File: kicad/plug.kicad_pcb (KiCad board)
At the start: 2 copper layers, 11 parts, among them J1 74320-1004, P1 HDMI_RECEPTACLE

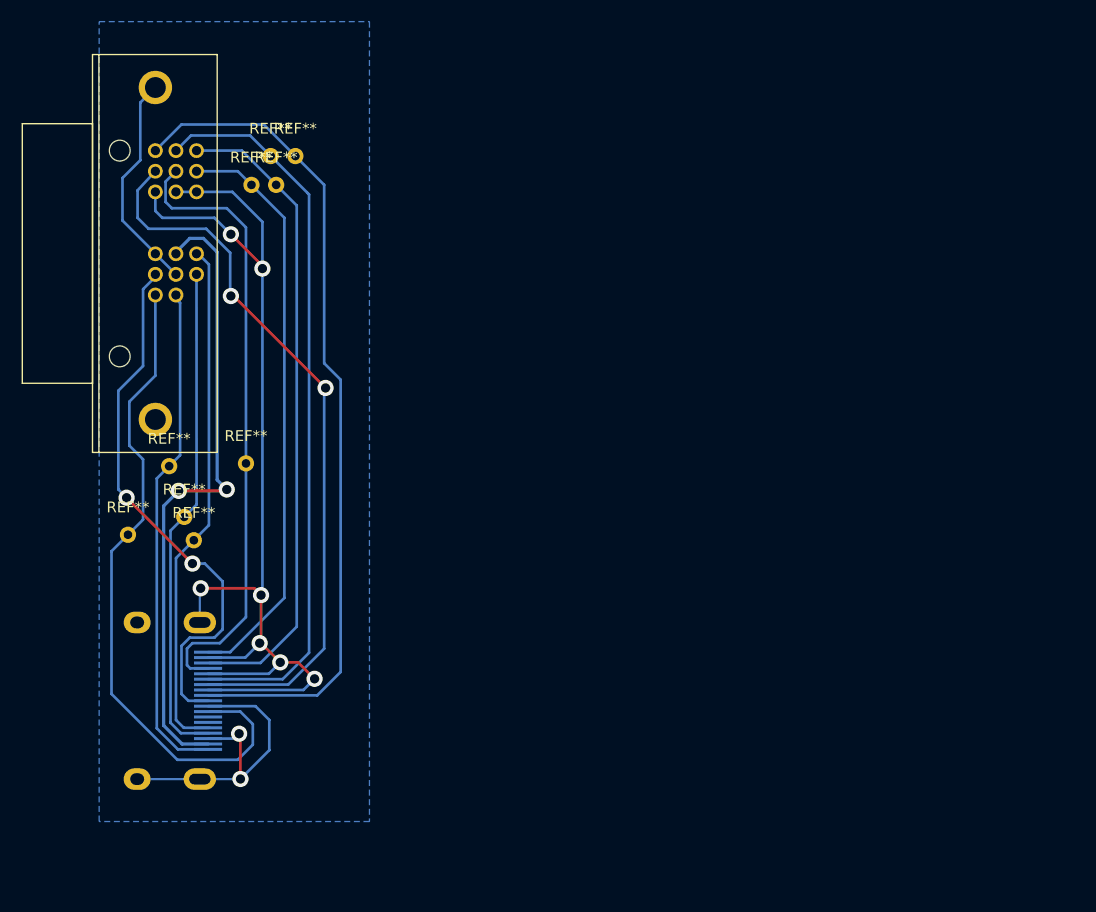
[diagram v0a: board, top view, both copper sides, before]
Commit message: simplier version since hdmi is a pain to manage.
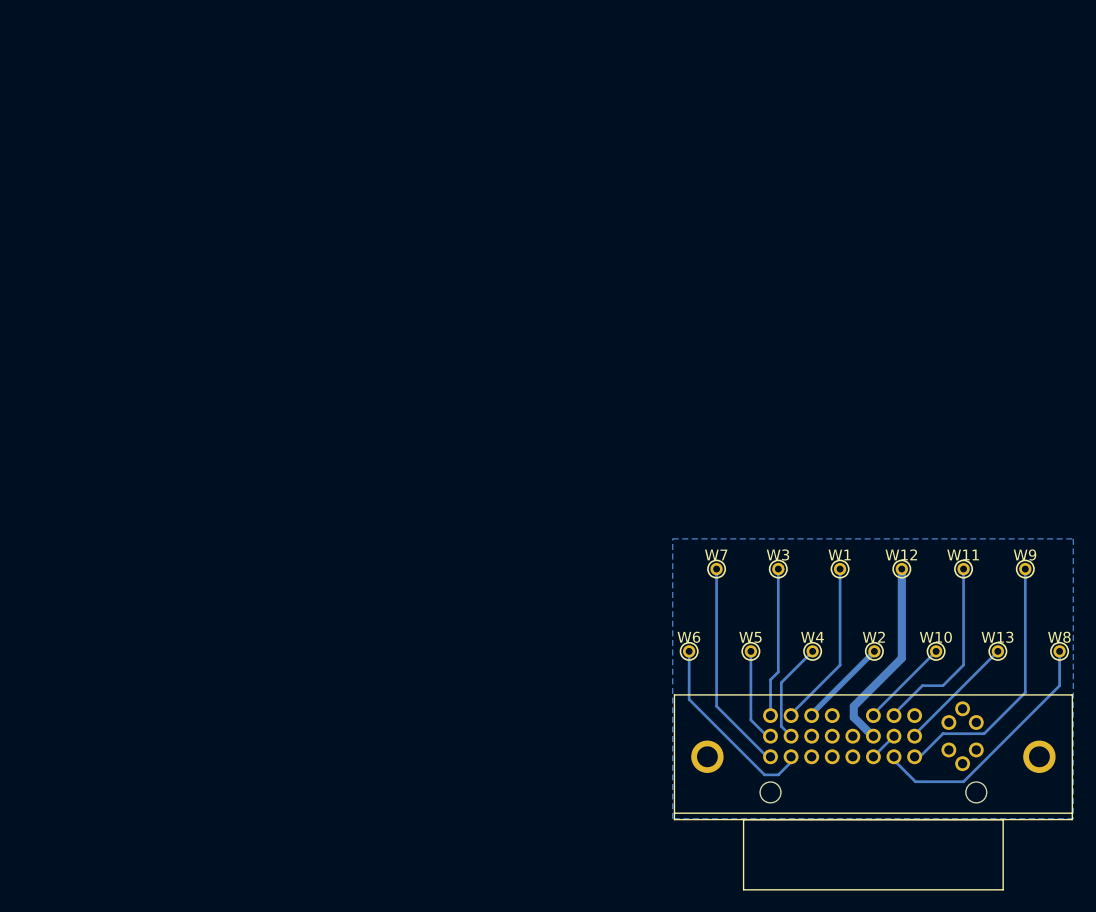
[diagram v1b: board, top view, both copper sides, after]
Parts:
- removed P1: HDMI_RECEPTACLE, project:HDMI_SMD
- removed REF** (x9): Measurement_Point_Round-TH_Small, Measurement_Points:Measurement_Point_Round-TH_Small
- added W1: TEST_1P, Connectors:PINTST, F.Cu at (154.9, 91.4)
- added W10: TEST_1P, Connectors:PINTST, F.Cu at (163.8, 99.1)
- added W11: TEST_1P, Connectors:PINTST, F.Cu at (166.4, 91.4)
- added W12: TEST_1P, Connectors:PINTST, F.Cu at (160.7, 91.4)
- added W13: TEST_1P, Connectors:PINTST, F.Cu at (169.5, 99.1)
- added W2: TEST_1P, Connectors:PINTST, F.Cu at (158.1, 99.1)
- added W3: TEST_1P, Connectors:PINTST, F.Cu at (149.2, 91.4)
- added W4: TEST_1P, Connectors:PINTST, F.Cu at (152.4, 99.1)
- added W5: TEST_1P, Connectors:PINTST, F.Cu at (146.7, 99.1)
- added W6: TEST_1P, Connectors:PINTST, F.Cu at (141.0, 99.1)
- added W7: TEST_1P, Connectors:PINTST, F.Cu at (143.5, 91.4)
- added W8: TEST_1P, Connectors:PINTST, F.Cu at (175.3, 99.1)
- added W9: TEST_1P, Connectors:PINTST, F.Cu at (172.1, 91.4)
- moved J1 73.9 mm to (148.5, 105.0), turned to 0 degrees
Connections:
- J1 pad 11: /GND -> GND
- J1 pad 15: /GND -> GND
- J1 pad 19: /GND -> GND
- J1 pad 22: /GND -> GND
- J1 pad 25: /GND -> GND
- J1 pad 3: /GND -> GND
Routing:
- net /GND: track 151.0 -> 0.00 mm, vias 9 -> 0
- net /D1-: track 67.9 -> 8.79 mm
- net /D0-: track 77.8 -> 19.6 mm
- net /D0+: track 67.7 -> 17.8 mm, vias 2 -> 0
- net /D1+: track 58.1 -> 9.43 mm
- net /D2-: track 59.8 -> 13.9 mm
- net /+5v: track 59.0 -> 18.1 mm, vias 2 -> 0
- net /DDCcl: track 48.4 -> 8.35 mm
- net /D2+: track 54.2 -> 15.4 mm
- net /CL-: track 62.2 -> 24.1 mm
- net /hotplug: track 46.8 -> 11.0 mm
- net /DDCdata: track 46.5 -> 17.3 mm
- net /CL+: track 51.9 -> 23.3 mm, vias 2 -> 0
- net GND: track 0.00 -> 11.0 mm
- added copper zone on B.Cu, net GND
- removed copper zone on B.Cu, net /GND
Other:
- net class 5v: trace_width 0.3 -> 0.75
- net class GND added: clearance 0, trace_width 0.5, via_dia 1.50114, via_drill 0.86106

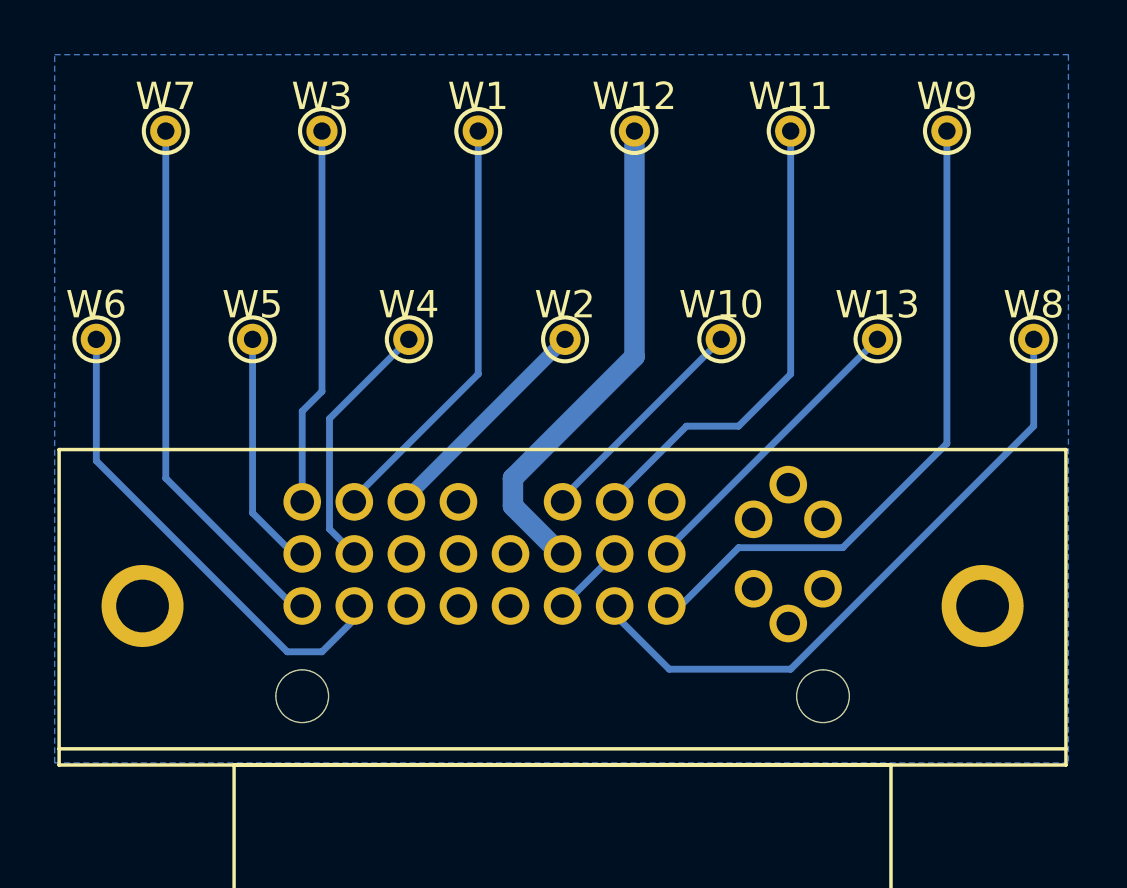
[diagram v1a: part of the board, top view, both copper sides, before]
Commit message: added pad footprint
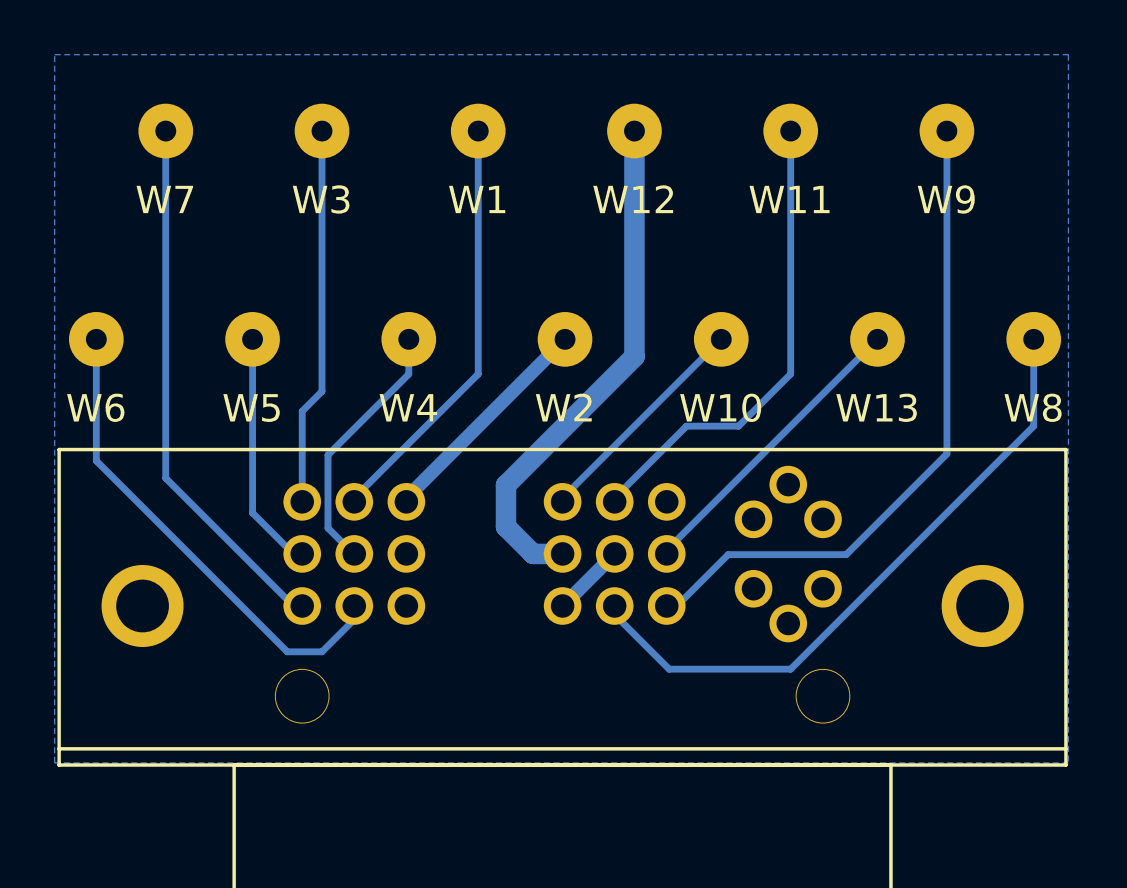
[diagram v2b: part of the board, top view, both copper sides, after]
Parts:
- W1, W10, W11, W12, W13, W2, W3, W4, W5, W6, W7, W8, W9: footprint Connectors:PINTST -> project:pad
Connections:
- J1 pad : (no net) -> GND
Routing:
- net /+5v: track 18.1 -> 19.0 mm

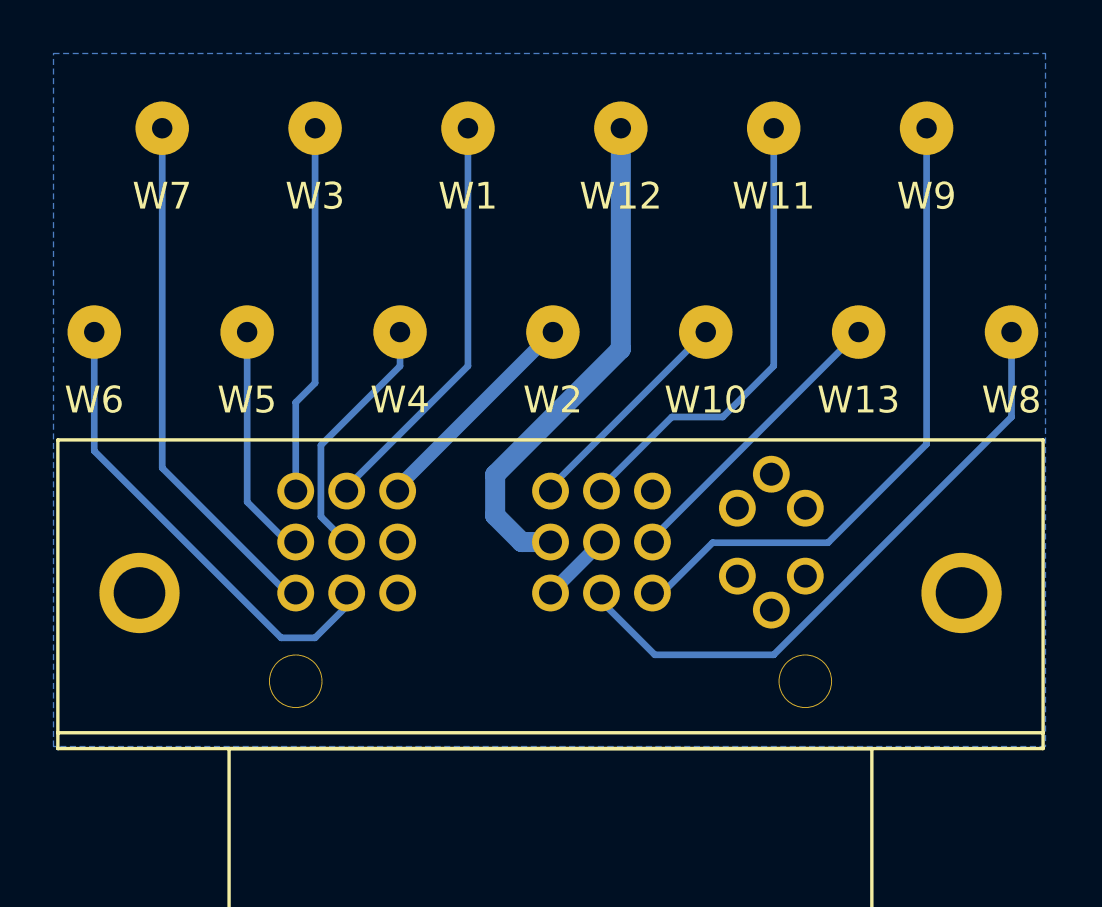
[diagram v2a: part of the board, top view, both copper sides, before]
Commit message: pads layout suits cable connexion better
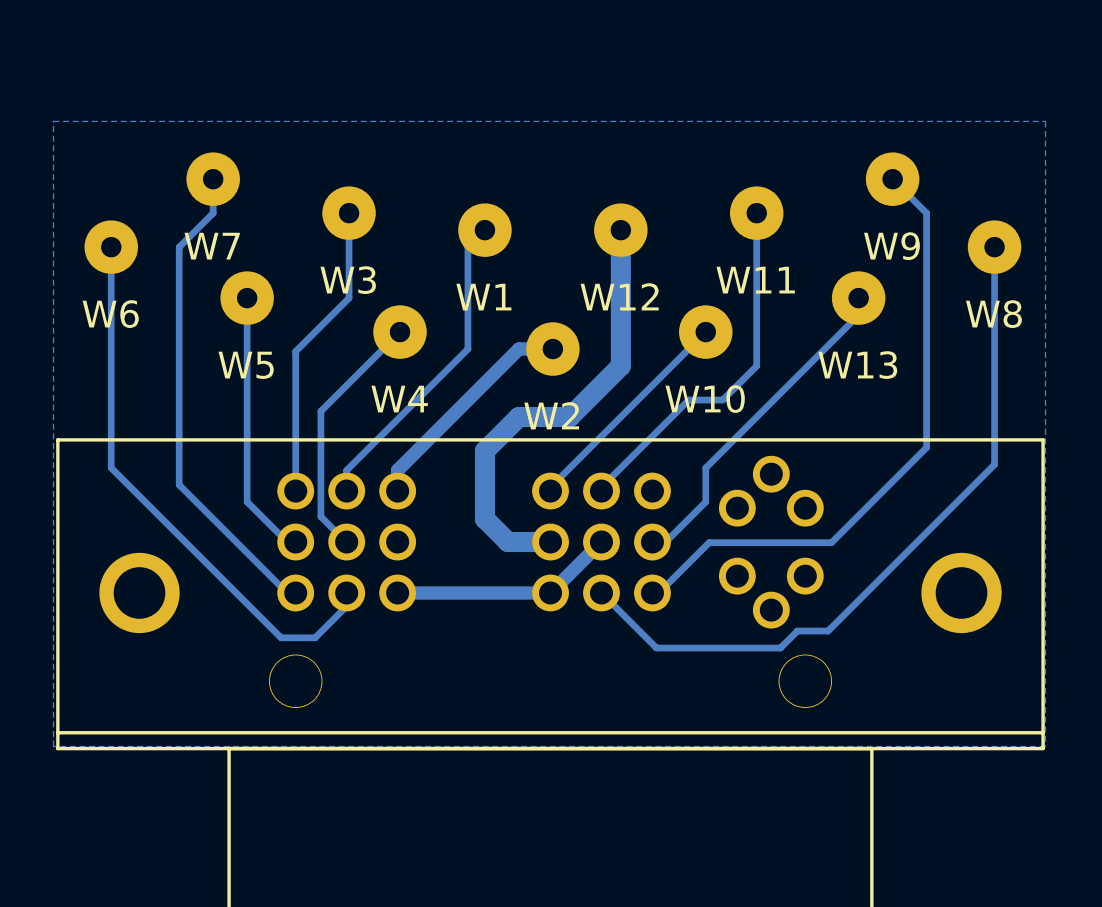
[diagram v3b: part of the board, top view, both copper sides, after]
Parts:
- moved W1 3.86 mm to (155.6, 95.2)
- moved W12 3.81 mm to (160.7, 95.2)
- moved W3 3.42 mm to (150.5, 94.6)
- moved W11 3.24 mm to (165.7, 94.6)
- moved W6 3.24 mm to (141.6, 95.9)
- moved W8 3.24 mm to (174.6, 95.9)
- moved W7 2.69 mm to (145.4, 93.3)
- moved W9 2.29 mm to (170.8, 93.3)
- moved W13 1.27 mm to (169.5, 97.8)
- moved W5 1.27 mm to (146.7, 97.8)
- moved W2 0.63 mm to (158.1, 99.7)
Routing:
- net GND: track 11.0 -> 17.0 mm
- net /DDCdata: track 17.3 -> 13.5 mm
- net /D2+: track 15.4 -> 11.9 mm
- net /CL+: track 23.3 -> 26.8 mm
- net /D0+: track 17.8 -> 20.7 mm
- net /D2-: track 13.9 -> 11.2 mm
- net /+5v: track 19.0 -> 16.9 mm
- net /D0-: track 19.6 -> 18.0 mm
- net /hotplug: track 11.0 -> 12.6 mm
- net /D1-: track 8.79 -> 10.1 mm
- net /CL-: track 24.4 -> 23.4 mm
